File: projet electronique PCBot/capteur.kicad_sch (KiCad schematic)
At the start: 3 parts, among them J2 nRF24, J3 TOF, U6 LSM6DSOX

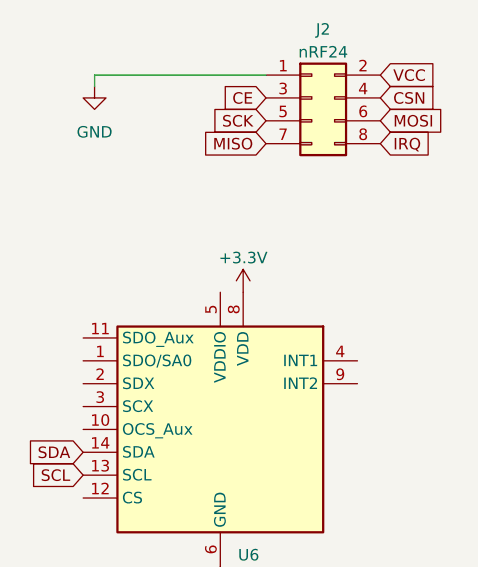
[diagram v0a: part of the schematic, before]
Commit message: Ajout de la feuille hiérarchique moteur
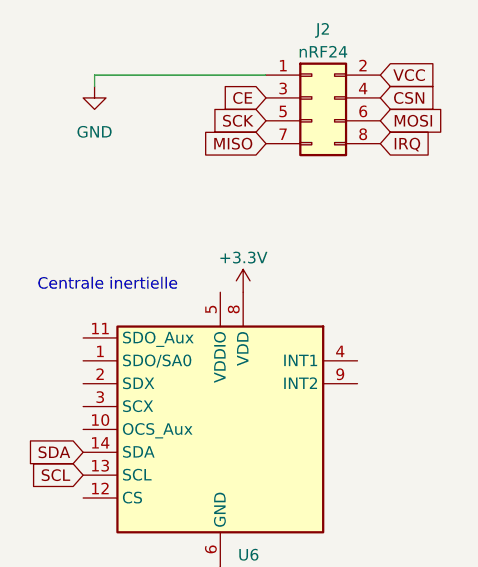
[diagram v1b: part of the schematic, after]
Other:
- note added: "Centrale inertielle"
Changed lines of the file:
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@@
     (stroke (width 0) (type default))
+  )
+  (text "Centrale inertielle\n" (at 83.82 96.52 0)
+    (effects (font (size 1.27 1.27)) (justify left bottom))
   )
   (global_label "IRQ" (shape input) (at 121.92 80.01 0) (fields_autoplaced)

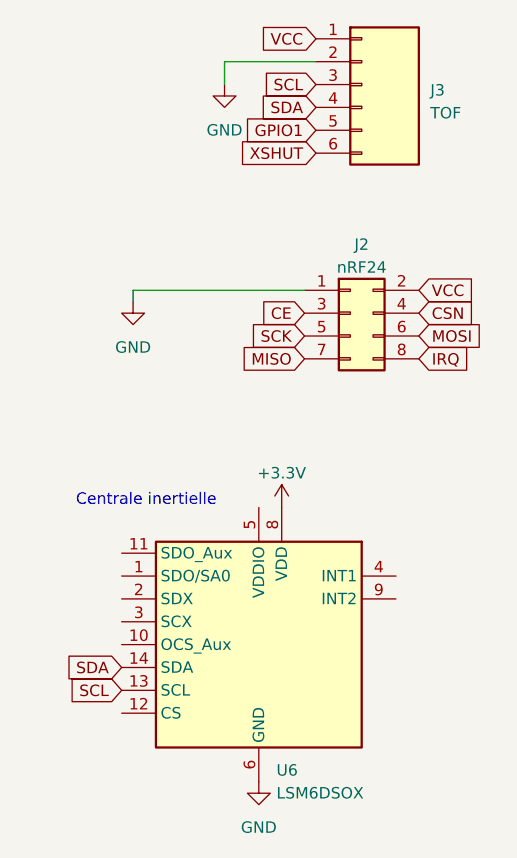
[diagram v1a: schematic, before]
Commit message: Modification des feuilles hiérarchiques et le main
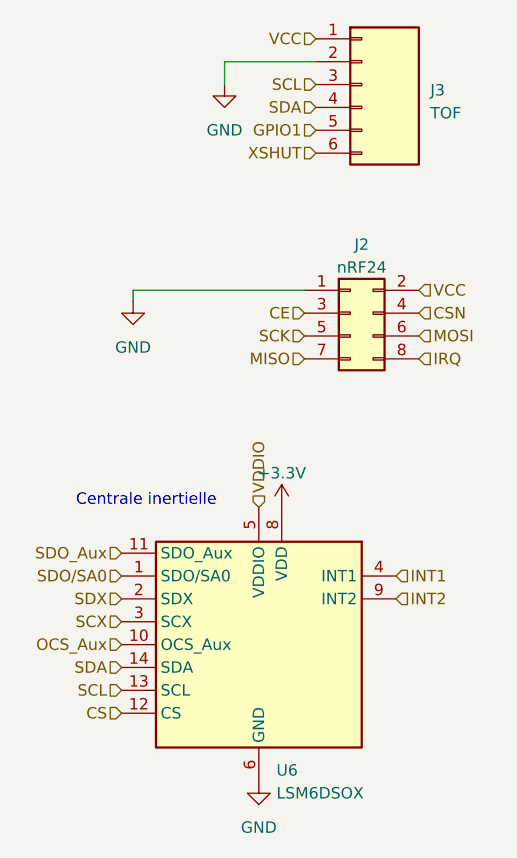
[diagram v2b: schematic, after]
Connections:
- net SDO/SA0: now reaches U6.1 (SDO/SA0)
- net OCS_Aux: now reaches U6.10 (OCS_Aux)
- net SDO_Aux: now reaches U6.11 (SDO_Aux)
- net CS: now reaches U6.12 (CS)
- net SDX: now reaches U6.2 (SDX)
- net SCX: now reaches U6.3 (SCX)
- net INT1: now reaches U6.4 (INT1)
- net VDDIO: now reaches U6.5 (VDDIO)
- net INT2: now reaches U6.9 (INT2)
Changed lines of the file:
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@@
     (effects (font (size 1.27 1.27)) (justify left bottom))
   )
-  (global_label "IRQ" (shape input) (at 121.92 80.01 0) (fields_autoplaced)
+  (hierarchical_label "GPIO1" (shape input) (at 110.49 54.61 180) (fields_autoplaced)
+    (effects (font (size 1.27 1.27)) (justify right))
+  )
+  (hierarchical_label "INT1" (shape input) (at 119.38 104.14 0) (fields_autoplaced)
     (effects (font (size 1.27 1.27)) (justify left))
-    (property "Intersheetrefs" "${INTERSHEET_REFS}" (at 128.0311 80.01 0)
-      (effects (font (size 1.27 1.27)) (justify left) hide)
-    )
   )
-  (global_label "SDA" (shape input) (at 88.9 114.3 180) (fields_autoplaced)
+  (hierarchical_label "IRQ" (shape input) (at 121.92 80.01 0) (fields_autoplaced)
+    (effects (font (size 1.27 1.27)) (justify left))
+  )
+  (hierarchical_label "VDDIO" (shape input) (at 104.14 96.52 90) (fields_autoplaced)
+    (effects (font (size 1.27 1.27)) (justify left))
+  )
+  (hierarchical_label "CS" (shape input) (at 88.9 119.38 180) (fields_autoplaced)
     (effects (font (size 1.27 1.27)) (justify right))
-    (property "Intersheetrefs" "${INTERSHEET_REFS}" (at 82.4261 114.3 0)
-      (effects (font (size 1.27 1.27)) (justify right) hide)
-    )
   )
-  (global_label "SCK" (shape input) (at 109.22 77.47 180) (fields_autoplaced)
+  (hierarchical_label "CE" (shape input) (at 109.22 74.93 180) (fields_autoplaced)
     (effects (font (size 1.27 1.27)) (justify right))
-    (property "Intersheetrefs" "${INTERSHEET_REFS}" (at 102.5647 77.47 0)
-      (effects (font (size 1.27 1.27)) (justify right) hide)
-    )
   )
-  (global_label "VCC" (shape input) (at 110.49 44.45 180) (fields_autoplaced)
+  (hierarchical_label "MOSI" (shape input) (at 121.92 77.47 0) (fields_autoplaced)
+    (effects (font (size 1.27 1.27)) (justify left))
+  )
+  (hierarchical_label "XSHUT" (shape input) (at 110.49 57.15 180) (fields_autoplaced)
     (effects (font (size 1.27 1.27)) (justify right))
-    (property "Intersheetrefs" "${INTERSHEET_REFS}" (at 103.9556 44.45 0)
-      (effects (font (size 1.27 1.27)) (justify right) hide)
-    )
   )
-  (global_label "GPIO1" (shape input) (at 110.49 54.61 180) (fields_autoplaced)
+  (hierarchical_label "SCL" (shape input) (at 88.9 116.84 180) (fields_autoplaced)
     (effects (font (size 1.27 1.27)) (justify right))
-    (property "Intersheetrefs" "${INTERSHEET_REFS}" (at 101.8994 54.61 0)
-      (effects (font (size 1.27 1.27)) (justify right) hide)
-    )
   )
-  (global_label "SCL" (shape input) (at 110.49 49.53 180) (fields_autoplaced)
+  (hierarchical_label "INT2" (shape input) (at 119.38 106.68 0) (fields_autoplaced)
+    (effects (font (size 1.27 1.27)) (justify left))
+  )
+  (hierarchical_label "SDA" (shape input) (at 110.49 52.07 180) (fields_autoplaced)
     (effects (font (size 1.27 1.27)) (justify right))
-    (property "Intersheetrefs" "${INTERSHEET_REFS}" (at 104.0766 49.53 0)
-      (effects (font (size 1.27 1.27)) (justify right) hide)
-    )
   )
-  (global_label "CSN" (shape input) (at 121.92 74.93 0) (fields_autoplaced)
+  (hierarchical_label "MISO" (shape input) (at 109.22 80.01 180) (fields_autoplaced)
+    (effects (font (size 1.27 1.27)) (justify right))
+  )
+  (hierarchical_label "SDO{slash}SA0" (shape input) (at 88.9 104.14 180) (fields_autoplaced)
+    (effects (font (size 1.27 1.27)) (justify right))
+  )
+  (hierarchical_label "VCC" (shape input) (at 121.92 72.39 0) (fields_autoplaced)
     (effects (font (size 1.27 1.27)) (justify left))
-    (property "Intersheetrefs" "${INTERSHEET_REFS}" (at 128.6358 74.93 0)
-      (effects (font (size 1.27 1.27)) (justify left) hide)
-    )
   )
-  (global_label "SCL" (shape input) (at 88.9 116.84 180) (fields_autoplaced)
+  (hierarchical_label "SDX" (shape input) (at 88.9 106.68 180) (fields_autoplaced)
     (effects (font (size 1.27 1.27)) (justify right))
-    (property "Intersheetrefs" "${INTERSHEET_REFS}" (at 82.4866 116.84 0)
-      (effects (font (size 1.27 1.27)) (justify right) hide)
-    )
   )
-  (global_label "MOSI" (shape input) (at 121.92 77.47 0) (fields_autoplaced)
+  (hierarchical_label "SCX" (shape input) (at 88.9 109.22 180) (fields_autoplaced)
+    (effects (font (size 1.27 1.27)) (justify right))
+  )
+  (hierarchical_label "SCK" (shape input) (at 109.22 77.47 180) (fields_autoplaced)
+    (effects (font (size 1.27 1.27)) (justify right))
+  )
+  (hierarchical_label "SDA" (shape input) (at 88.9 114.3 180) (fields_autoplaced)
+    (effects (font (size 1.27 1.27)) (justify right))
+  )
+  (hierarchical_label "SCL" (shape input) (at 110.49 49.53 180) (fields_autoplaced)
+    (effects (font (size 1.27 1.27)) (justify right))
+  )
+  (hierarchical_label "OCS_Aux" (shape input) (at 88.9 111.76 180) (fields_autoplaced)
+    (effects (font (size 1.27 1.27)) (justify right))
+  )
+  (hierarchical_label "SDO_Aux" (shape input) (at 88.9 101.6 180) (fields_autoplaced)
+    (effects (font (size 1.27 1.27)) (justify right))
+  )
+  (hierarchical_label "CSN" (shape input) (at 121.92 74.93 0) (fields_autoplaced)
     (effects (font (size 1.27 1.27)) (justify left))
-    (property "Intersheetrefs" "${INTERSHEET_REFS}" (at 129.422 77.47 0)
-      (effects (font (size 1.27 1.27)) (justify left) hide)
-    )
   )
-  (global_label "CE" (shape input) (at 109.22 74.93 180) (fields_autoplaced)
+  (hierarchical_label "VCC" (shape input) (at 110.49 44.45 180) (fields_autoplaced)
     (effects (font (size 1.27 1.27)) (justify right))
-    (property "Intersheetrefs" "${INTERSHEET_REFS}" (at 103.8952 74.93 0)
-      (effects (font (size 1.27 1.27)) (justify right) hide)
-    )
-  )
-  (global_label "MISO" (shape input) (at 109.22 80.01 180) (fields_autoplaced)
-    (effects (font (size 1.27 1.27)) (justify right))
-    (property "Intersheetrefs" "${INTERSHEET_REFS}" (at 101.718 80.01 0)
-      (effects (font (size 1.27 1.27)) (justify right) hide)
-    )
-  )
-  (global_label "XSHUT" (shape input) (at 110.49 57.15 180) (fields_autoplaced)
-    (effects (font (size 1.27 1.27)) (justify right))
-    (property "Intersheetrefs" "${INTERSHEET_REFS}" (at 101.5366 57.15 0)
-      (effects (font (size 1.27 1.27)) (justify right) hide)
-    )
-  )
-  (global_label "SDA" (shape input) (at 110.49 52.07 180) (fields_autoplaced)
-    (effects (font (size 1.27 1.27)) (justify right))
-    (property "Intersheetrefs" "${INTERSHEET_REFS}" (at 104.0161 52.07 0)
-      (effects (font (size 1.27 1.27)) (justify right) hide)
-    )
-  )
-  (global_label "VCC" (shape input) (at 121.92 72.39 0) (fields_autoplaced)
-    (effects (font (size 1.27 1.27)) (justify left))
-    (property "Intersheetrefs" "${INTERSHEET_REFS}" (at 128.4544 72.39 0)
-      (effects (font (size 1.27 1.27)) (justify left) hide)
-    )
   )
   (symbol (lib_id "power:GND") (at 100.33 49.53 0) (unit 1)

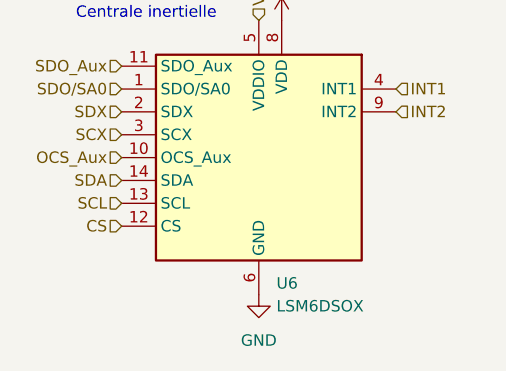
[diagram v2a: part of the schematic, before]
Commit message: ajout de la feuille connecteurs
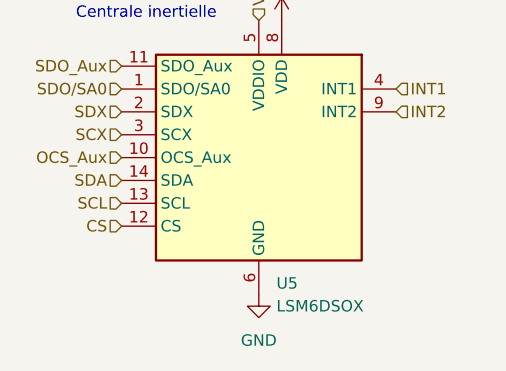
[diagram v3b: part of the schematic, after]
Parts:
- renumbered U6 to U5

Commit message: modification de la feuille capteurs
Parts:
- added J4, J6: TOF, symbol pcbot_lib:TOF
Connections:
- net +3.3V: now also J2.2 (Pin_2)
- net GPIO1: now also J4.5 (GPIO1), J6.5 (GPIO1)
- net SCL: now also J4.3 (SCL), J6.3 (SCL)
- net SDA: now also J4.4 (SDA), J6.4 (SDA)
- net VCC: no longer J2.2 (Pin_2)
- net XSHUT: now also J4.6 (XST), J6.6 (XST)
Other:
- note added: "(VCC)"
- note added: "cf google doc partie stm32 pour branchements des pins de nRF24"
- moved on the sheet: J2, U5

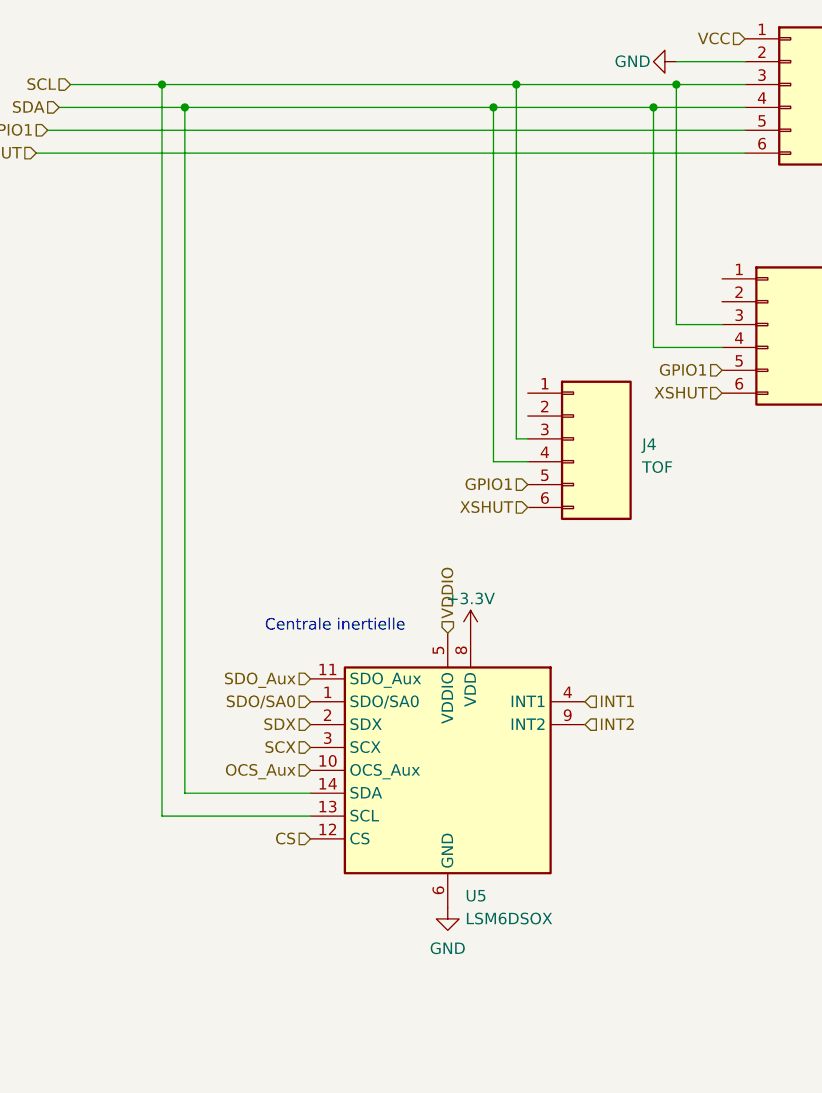
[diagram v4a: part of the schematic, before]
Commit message: modifications dans feuilles stm et capteurs
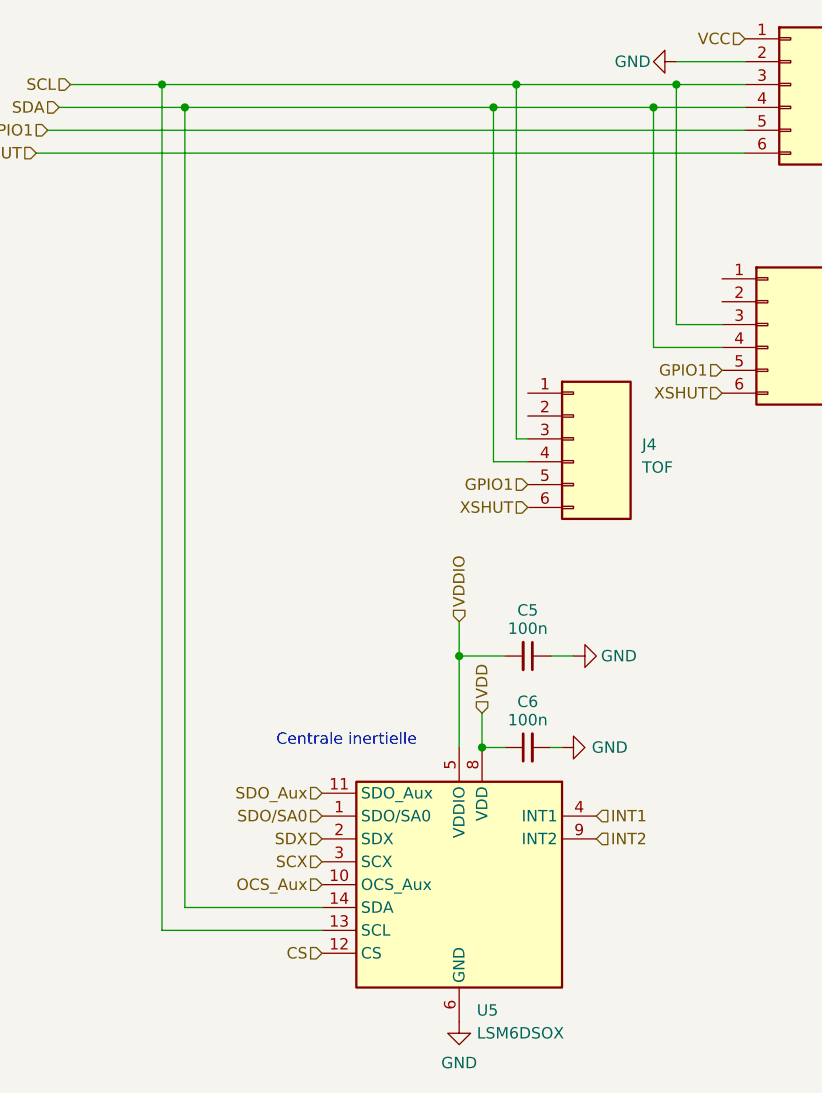
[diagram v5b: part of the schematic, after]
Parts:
- added C5, C6: 100n, symbol Device:C_Small
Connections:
- net +3.3V: no longer U5.8 (VDD)
- net GND: now also C5.1, C6.2
- net VDDIO: now also C5.2
- new net VDD: C6.1, U5.8 (VDD)
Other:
- moved on the sheet: U5

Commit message: modif de flo capteur
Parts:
- added U1: LSM6DSM, Package_LGA:LGA-14_3x2.5mm_P0.5mm_LayoutBorder3x4y, symbol Sensor_Motion:LSM6DSM
- renumbered J3 to J1, J6 to J2, J4 to J3
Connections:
- net GND: now also J2.2 (GND), J3.2 (GND)
- net VCC: now also J2.1 (3.3V), J3.1 (3.3V)
- removed net GPIO1: J1.5 (GPIO1), J2.5 (GPIO1), J3.5 (GPIO1)
- net OCS_Aux: no longer names the net of U5.10 (OCS_Aux)
- net SCX: no longer names the net of U5.3 (SCX)
- net SDO_Aux: no longer names the net of U5.11 (SDO_Aux)
- net SDO/SA0: no longer names the net of U5.1 (SDO/SA0)
- net SDX: no longer names the net of U5.2 (SDX)
- removed net XSHUT: J1.6 (XST), J2.6 (XST), J3.6 (XST)
- new net: U1.6 (GND), U1.7 (GND)
- new net TOF1_GPIO1: J1.5 (GPIO1)
- new net TOF1_XSHUT: J1.6 (XST)
- new net TOF2_GPIO1: J2.5 (GPIO1)
- new net TOF2_XSHUT: J2.6 (XST)
- new net TOF3_GPIO1: J3.5 (GPIO1)
- new net TOF3_XSHUT: J3.6 (XST)
- no-connect marks 0 -> 4
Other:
- moved on the sheet: J2

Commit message: modif
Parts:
- renumbered J1 to J3, J3 to J4, J2 to J6, U1 to U?
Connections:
- net SDO/SA0: now reaches U5.1 (SDO/SA0)
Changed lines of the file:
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@@
+		)
+	)
+	(hierarchical_label "SDO{slash}SA0"
+		(shape input)
+		(at 63.5 130.81 180)
+		(effects
+			(font
+				(size 1.27 1.27)
+			)
+			(justify right)
 		)
 	)
@@
 		(on_board yes)
 		(dnp no)
-		(property "Reference" "#PWR?"
+		(property "Reference" "#PWR09"
 			(at 96.52 46.99 0)
 			(effects
@@
 		(dnp no)
 		(fields_autoplaced yes)
-		(property "Reference" "J3"
+		(property "Reference" "J4"
 			(at 99.06 88.8999 0)
 			(effects
@@
 		(on_board yes)
 		(dnp no)
-		(property "Reference" "#PWR?"
+		(property "Reference" "#PWR021"
 			(at 167.64 102.87 0)
 			(effects
@@
 		(on_board yes)
 		(dnp no)
-		(property "Reference" "C?"
+		(property "Reference" "C6"
 			(at 86.36 118.11 90)
 			(effects
@@
 		(on_board yes)
 		(dnp no)
-		(property "Reference" "#PWR?"
+		(property "Reference" "#PWR03"
 			(at 96.52 123.19 0)
 			(effects
@@
 		(dnp no)
 		(fields_autoplaced yes)
-		(property "Reference" "U?"
+		(property "Reference" "U5"
 			(at 80.6959 152.4 0)
 			(effects
@@
 		(dnp no)
 		(fields_autoplaced yes)
-		(property "Reference" "J1"
+		(property "Reference" "J3"
 			(at 123.19 49.5299 0)
 			(effects
@@
 		(on_board yes)
 		(dnp no)
-		(property "Reference" "#PWR?"
+		(property "Reference" "#PWR06"
 			(at 139.7 110.49 0)
 			(effects
@@
 		(on_board yes)
 		(dnp no)
-		(property "Reference" "#PWR?"
+		(property "Reference" "#PWR02"
 			(at 97.79 113.03 0)
 			(effects
@@
 		(on_board yes)
 		(dnp no)
-		(property "Reference" "#PWR01"
+		(property "Reference" "#PWR?"
 			(at 107.95 73.66 0)
 			(effects
@@
 		)
 		(instances
+			(project "projet electronique PCBot"
+				(path "/210be09d-86cd-4faa-bb91-cc54c5972517/93c3b10c-af7a-4302-b763-bec1b6a7b44e"
+					(reference "#PWR?")
+					(unit 1)
+				)
+			)
 			(project "capteur"
 				(path "/c8d670ff-7238-40a1-bca3-b6d77bee1c63"
@@
 		(dnp no)
 		(fields_autoplaced yes)
-		(property "Reference" "U1"
+		(property "Reference" "U?"
 			(at 115.1733 173.99 0)
 			(effects
@@
 		)
 		(instances
+			(project "projet electronique PCBot"
+				(path "/210be09d-86cd-4faa-bb91-cc54c5972517/93c3b10c-af7a-4302-b763-bec1b6a7b44e"
+					(reference "U?")
+					(unit 1)
+				)
+			)
 			(project ""
 				(path "/c8d670ff-7238-40a1-bca3-b6d77bee1c63"
@@
 		(on_board yes)
 		(dnp no)
-		(property "Reference" "#PWR?"
+		(property "Reference" "#PWR010"
 			(at 78.74 160.02 0)
 			(effects
@@
 		(dnp no)
 		(fields_autoplaced yes)
-		(property "Reference" "J?"
+		(property "Reference" "J2"
 			(at 165.1 97.79 0)
 			(effects
@@
 		(on_board yes)
 		(dnp no)
-		(property "Reference" "C?"
+		(property "Reference" "C5"
 			(at 86.36 107.95 90)
 			(effects
@@
 		(on_board yes)
 		(dnp no)
-		(property "Reference" "#PWR02"
+		(property "Reference" "#PWR?"
 			(at 74.93 86.36 0)
 			(effects
@@
 		)
 		(instances
+			(project "projet electronique PCBot"
+				(path "/210be09d-86cd-4faa-bb91-cc54c5972517/93c3b10c-af7a-4302-b763-bec1b6a7b44e"
+					(reference "#PWR?")
+					(unit 1)
+				)
+			)
 			(project "capteur"
 				(path "/c8d670ff-7238-40a1-bca3-b6d77bee1c63"
@@
 		(dnp no)
 		(fields_autoplaced yes)
-		(property "Reference" "J2"
+		(property "Reference" "J6"
 			(at 127 76.1999 0)
 			(effects

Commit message: modif de capteurs le vrai de vrai
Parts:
- removed U?: LSM6DSM, Package_LGA:LGA-14_3x2.5mm_P0.5mm_LayoutBorder3x4y, symbol Sensor_Motion:LSM6DSM
- renumbered J3 to J1, J6 to J2, J4 to J3
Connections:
- net CS is gone; now on net +3.3V: U5.12 (CS)
- net SDO/SA0 is gone; now on net GND: U5.1 (SDO/SA0)
- net VDD is gone; now on net +3.3V: C6.1, U5.8 (VDD)
- net VDDIO is gone; now on net +3.3V: C5.2, U5.5 (VDDIO)
- net INT1: no longer names the net of U5.4 (INT1)
- net INT2: no longer names the net of U5.9 (INT2)
- no-connect marks 4 -> 6
